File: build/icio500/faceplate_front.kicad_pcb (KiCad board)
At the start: 2 copper layers, 38.1 x 133.3 mm, 3 parts, among them U2 PinHeader_2x07_P2.54mm_Vertic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, U4 TSSOP-24_4.4x7.8mm_P0.65mm

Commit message: faceplate mockupo
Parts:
- removed C3: C_0603_1608Metric, C_0603_1608Metric
- removed U2: PinHeader_2x07_P2.54mm_Vertical, PinHeader_2x07_P2.54mm_Vertical
- removed U4: TSSOP-24_4.4x7.8mm_P0.65mm, TSSOP-24_4.4x7.8mm_P0.65mm
- added ?: , EncoderGraphicGeometric, F.Cu at (19.1, 109.3)
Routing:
- removed copper zone on F.Cu, net (none)
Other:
- copper layers 2 -> 4
- board text removed: "A"
- board text removed: "B"
- board text removed: "G"
- board text removed: "MODE"
- board text removed: "R"
- board text removed: "SEQ"
- board text removed: "SHIFT"
- board text removed: "SYNC"
- board text removed: "TAP / TEMPO"

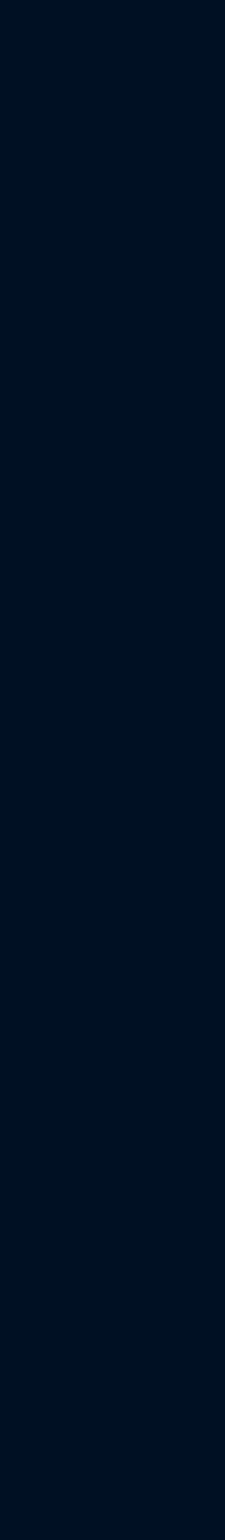
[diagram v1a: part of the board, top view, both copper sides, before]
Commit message: Clean up repo, add mounting holes to faceplate for mating, and assign nets/zones on satellite board via python
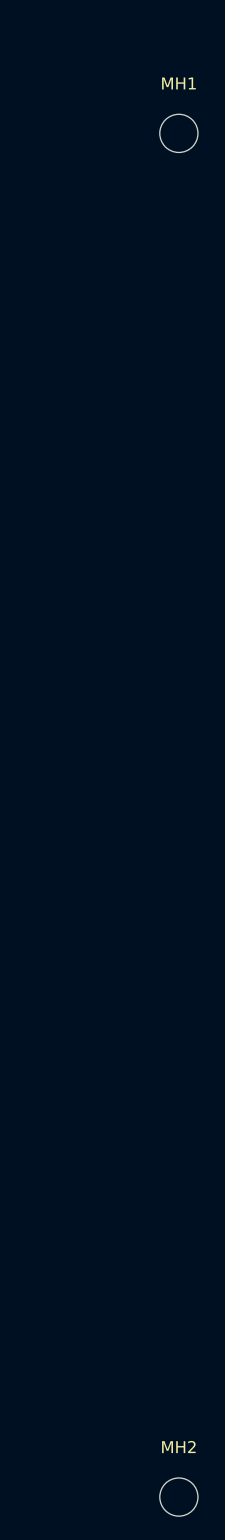
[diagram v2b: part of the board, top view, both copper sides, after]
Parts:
- added MH1: MountingHole_3.2mm_M3, MountingHole_3.2mm_M3, F.Cu at (119.0, 109.5)
- added MH2: MountingHole_3.2mm_M3, MountingHole_3.2mm_M3, F.Cu at (119.0, 223.8)
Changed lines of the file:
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@@
 		)
+	)
+	(footprint "MountingHole_3.2mm_M3"
+		(layer "F.Cu")
+		(at 119.05 109.5)
+		(descr "Mounting Hole 3.2mm, M3, no annular, generated by kicad-footprint-generator mountinghole.py")
+		(tags "mountinghole M3")
+		(property "Reference" "MH1"
+			(at 0 -4.15 0)
+			(layer "F.SilkS")
+			(effects
+				(font
+					(size 1 1)
+					(thickness 0.15)
+				)
+			)
+		)
+		(property "Value" "MountingHole_3.2mm_M3"
+			(at 0 4.15 0)
+			(layer "F.Fab")
+			(effects
+				(font
+					(size 1 1)
+					(thickness 0.15)
+				)
+			)
+		)
+		(property "Datasheet" ""
+			(at 0 0 0)
+			(layer "F.Fab")
+			(hide yes)
+			(effects
+				(font
+					(size 1.27 1.27)
+				)
+			)
+		)
+		(property "Description" ""
+			(at 0 0 0)
+			(layer "F.Fab")
+			(hide yes)
+			(effects
+				(font
+					(size 1.27 1.27)
+				)
+			)
+		)
+		(property "KiLib_Generator" "mounting_hardware/mounting_hole"
+			(at 0 0 0)
+			(layer "F.SilkS")
+			(hide yes)
+			(effects
+				(font
+					(size 1 1)
+					(thickness 0.15)
+				)
+			)
+		)
+		(attr exclude_from_pos_files exclude_from_bom)
+		(duplicate_pad_numbers_are_jumpers no)
+		(fp_circle
+			(center 0 0)
+			(end 3.2 0)
+			(stroke
+				(width 0.15)
+				(type solid)
+			)
+			(fill no)
+			(layer "Cmts.User")
+		)
+		(fp_circle
+			(center 0 0)
+			(end 3.45 0)
+			(stroke
+				(width 0.05)
+				(type solid)
+			)
+			(fill no)
+			(layer "F.CrtYd")
+		)
+		(fp_text user "${REFERENCE}"
+			(at 0 0 0)
+			(layer "F.Fab")
+			(effects
+				(font
+					(size 1 1)
+					(thickness 0.15)
+				)
+			)
+		)
+		(pad "" np_thru_hole circle
+			(at 0 0)
+			(size 3.2 3.2)
+			(drill 3.2)
+			(layers "*.Cu" "*.Mask")
+		)
+		(embedded_fonts no)
 	)
 	(footprint "EncoderGraphicGeometric"
@@
 		)
 		(embedded_fonts no)
+	)
+	(footprint "MountingHole_3.2mm_M3"
+		(layer "F.Cu")
+		(at 119.05 223.85)
+		(descr "Mounting Hole 3.2mm, M3, no annular, generated by kicad-footprint-generator mountinghole.py")
+		(tags "mountinghole M3")
+		(property "Reference" "MH2"
+			(at 0 -4.15 0)
+			(layer "F.SilkS")
+			(effects
+				(font
+					(size 1 1)
+					(thickness 0.15)
+				)
+			)
+		)
+		(property "Value" "MountingHole_3.2mm_M3"
+			(at 0 4.15 0)
+			(layer "F.Fab")
+			(effects
+				(font
+					(size 1 1)
+					(thickness 0.15)
+				)
+			)
+		)
+		(property "Datasheet" ""
+			(at 0 0 0)
+			(layer "F.Fab")
+			(hide yes)
+			(effects
+				(font
+					(size 1.27 1.27)
+				)
+			)
+		)
+		(property "Description" ""
+			(at 0 0 0)
+			(layer "F.Fab")
+			(hide yes)
+			(effects
+				(font
+					(size 1.27 1.27)
+				)
+			)
+		)
+		(property "KiLib_Generator" "mounting_hardware/mounting_hole"
+			(at 0 0 0)
+			(layer "F.SilkS")
+			(hide yes)
+			(effects
+				(font
+					(size 1 1)
+					(thickness 0.15)
+				)
+			)
+		)
+		(attr exclude_from_pos_files exclude_from_bom)
+		(duplicate_pad_numbers_are_jumpers no)
+		(fp_circle
+			(center 0 0)
+			(end 3.2 0)
+			(stroke
+				(width 0.15)
+				(type solid)
+			)
+			(fill no)
+			(layer "Cmts.User")
+		)
+		(fp_circle
+			(center 0 0)
+			(end 3.45 0)
+			(stroke
+				(width 0.05)
+				(type solid)
+			)
+			(fill no)
+			(layer "F.CrtYd")
+		)
+		(fp_text user "${REFERENCE}"
+			(at 0 0 0)
+			(layer "F.Fab")
+			(effects
+				(font
+					(size 1 1)
+					(thickness 0.15)
+				)
+			)
+		)
+		(pad "" np_thru_hole circle
+			(at 0 0)
+			(size 3.2 3.2)
+			(drill 3.2)
+			(layers "*.Cu" "*.Mask")
+		)
+		(embedded_fonts no)

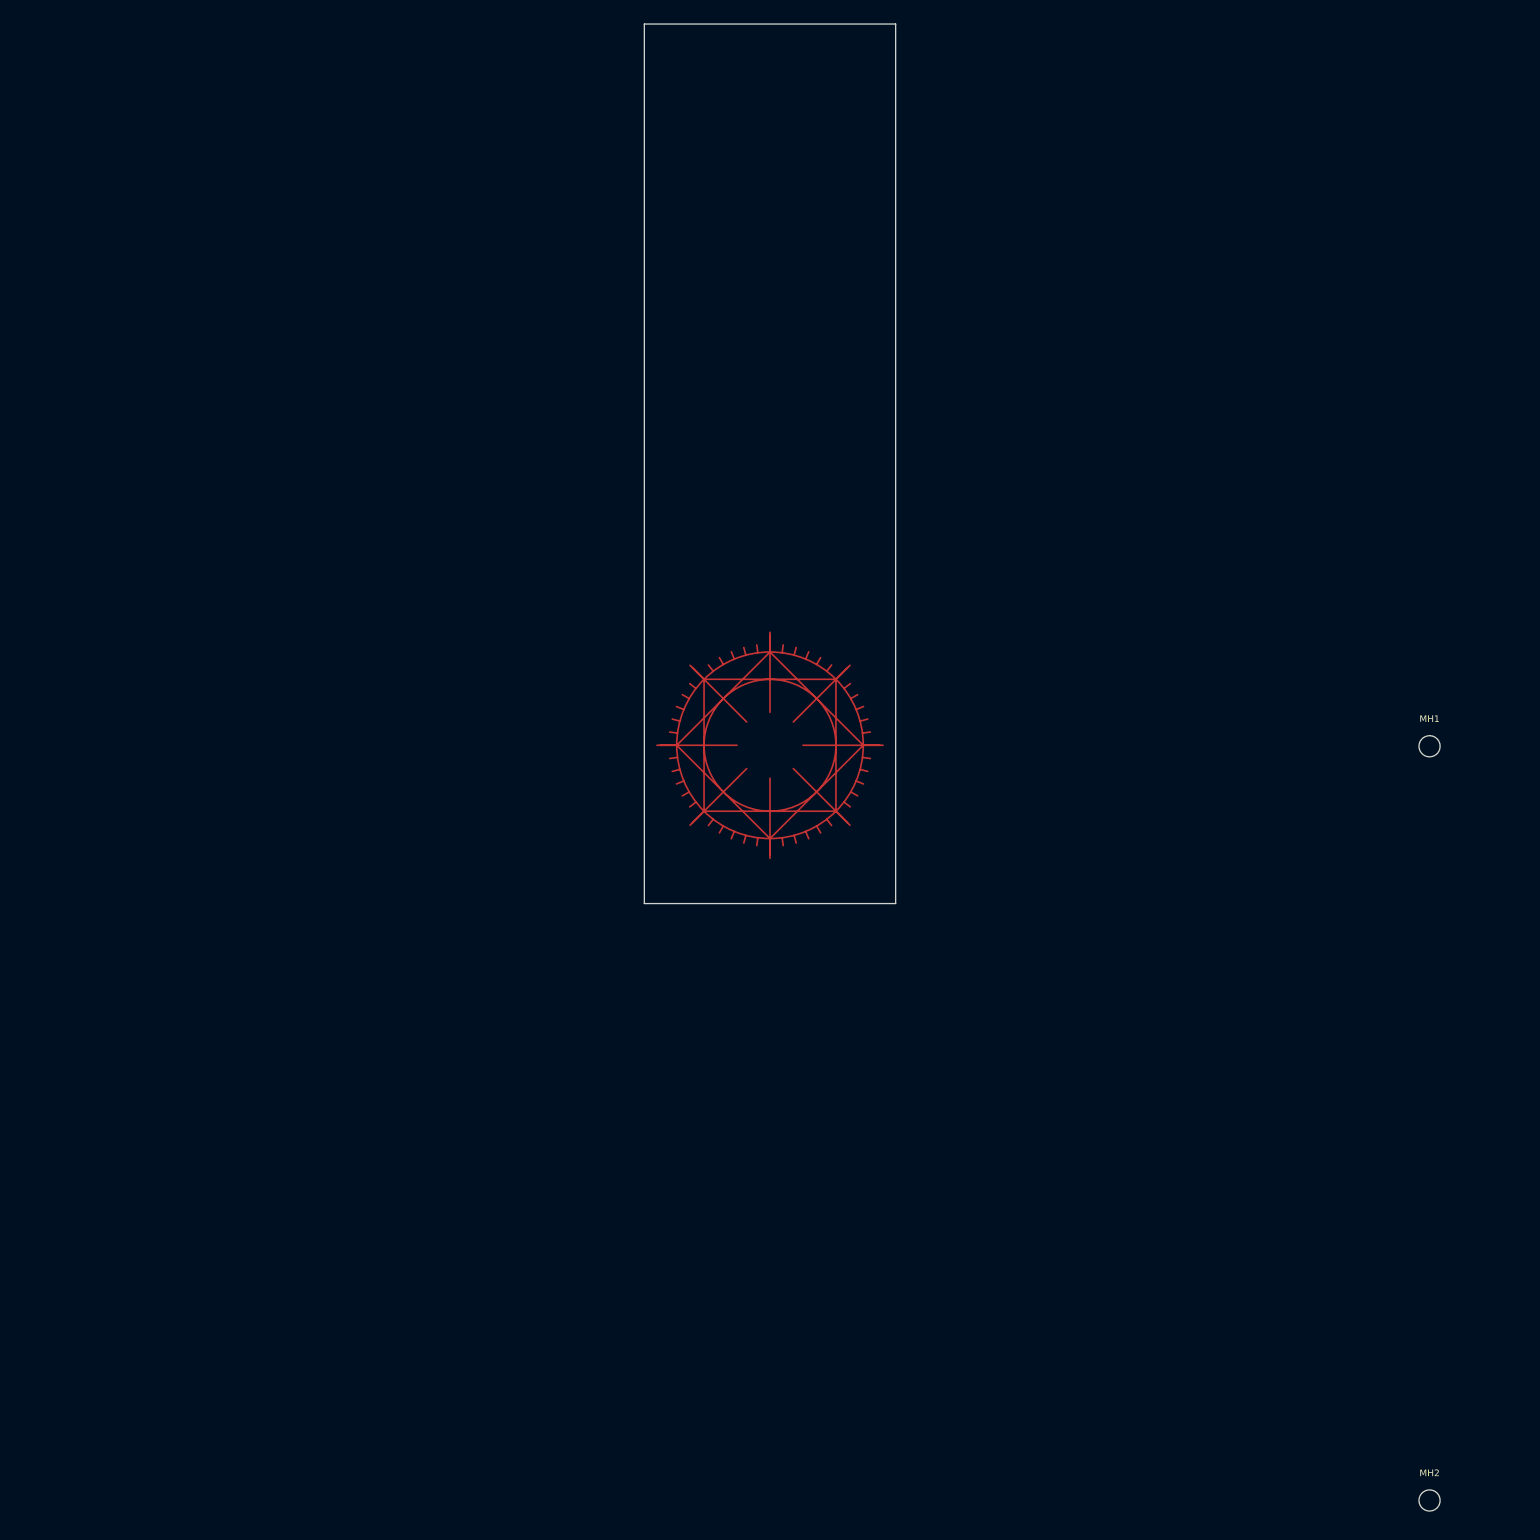
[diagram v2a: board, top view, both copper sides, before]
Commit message: Finalize VPR-500 dimensions and faceplate silkscreen
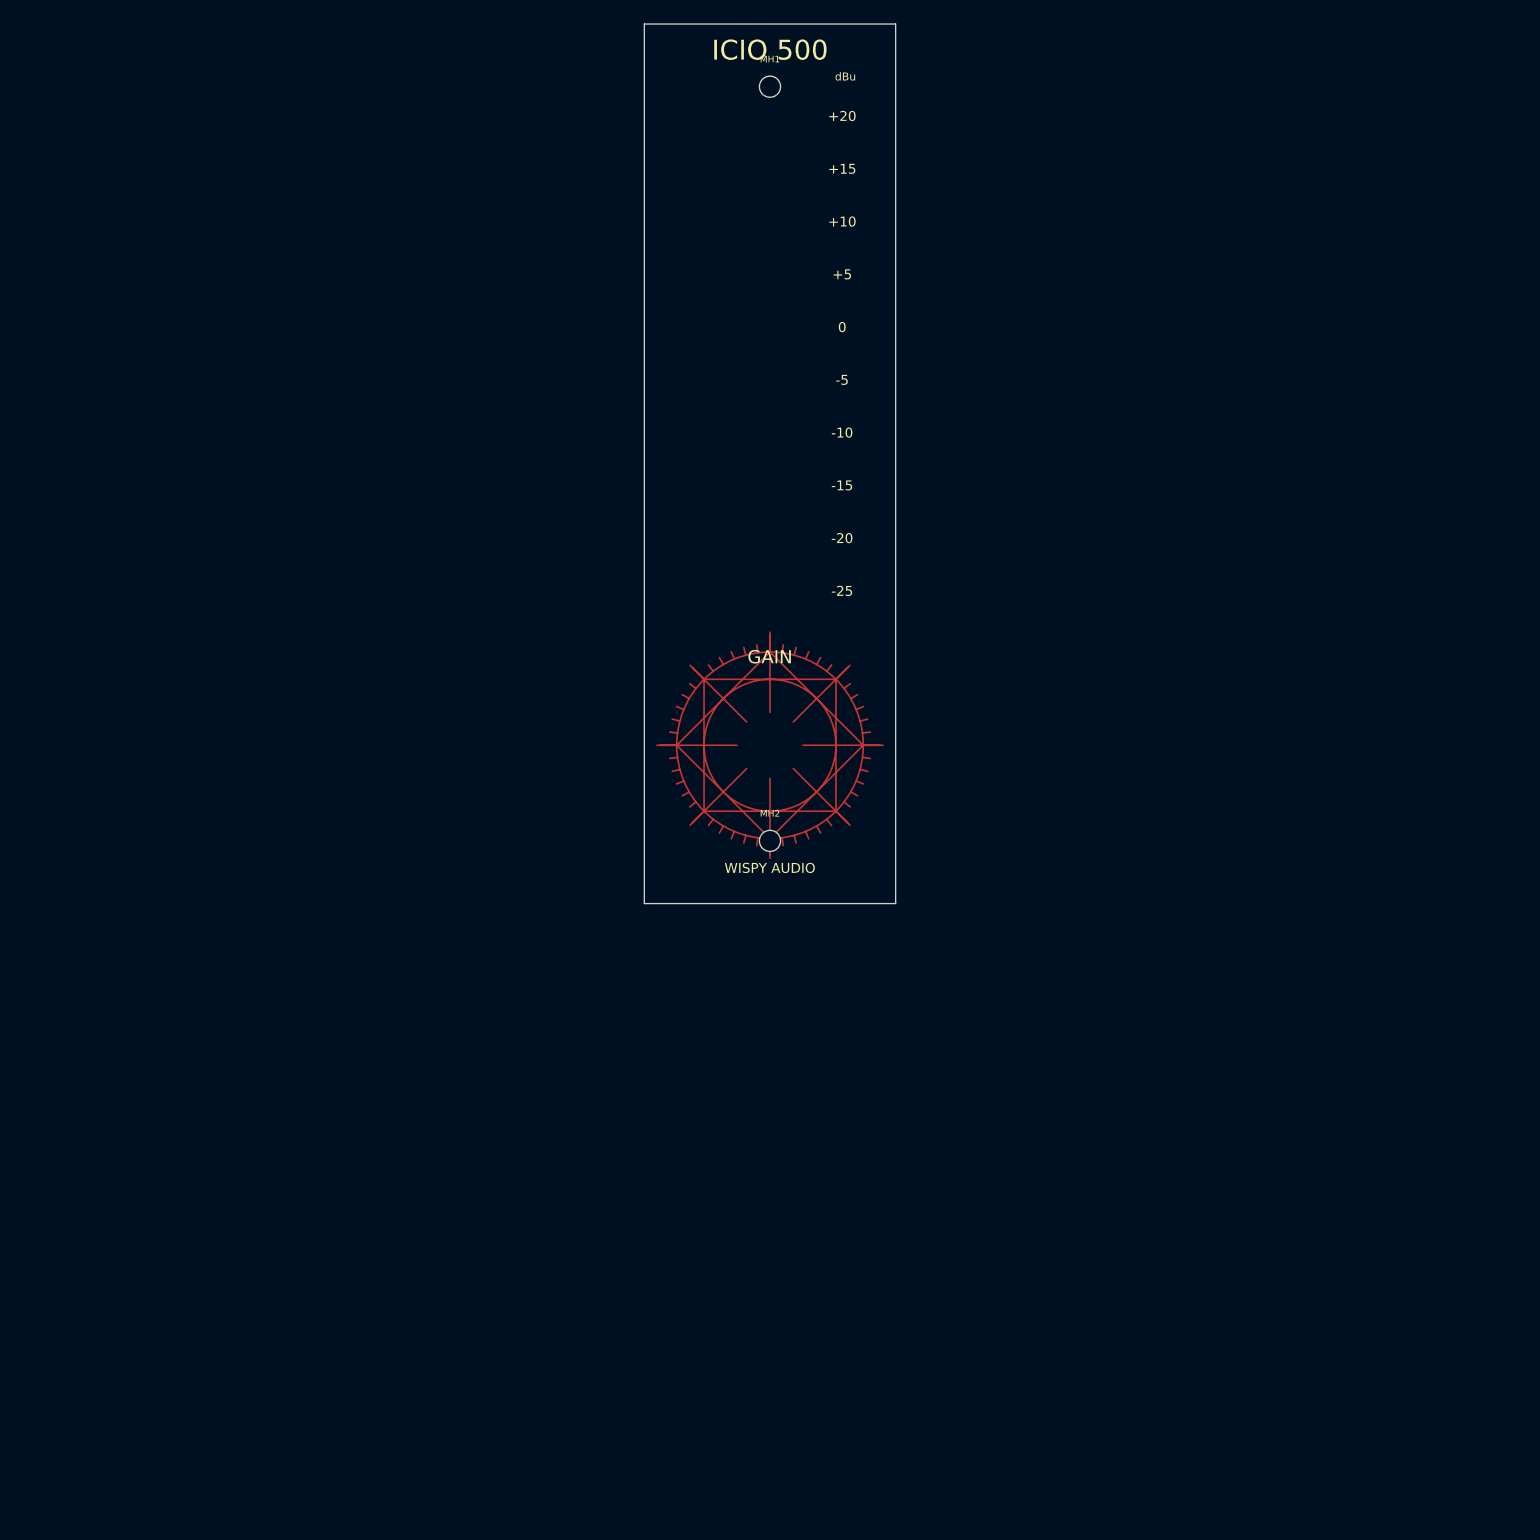
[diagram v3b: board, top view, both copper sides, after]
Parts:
- moved MH1 141.4 mm to (19.1, 9.50)
- moved MH2 141.4 mm to (19.1, 123.8)
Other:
- board text added: "+10"
- board text added: "+15"
- board text added: "+20"
- board text added: "+5"
- board text added: "-10"
- board text added: "-15"
- board text added: "-20"
- board text added: "-25"
- board text added: "-5"
- board text added: "0"
- board text added: "GAIN"
- board text added: "ICIO 500"
- board text added: "WISPY AUDIO"
- board text added: "dBu"
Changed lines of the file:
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@@
 	(footprint "MountingHole_3.2mm_M3"
 		(layer "F.Cu")
-		(at 119.05 109.5)
+		(at 19.05 9.5)
 		(descr "Mounting Hole 3.2mm, M3, no annular, generated by kicad-footprint-generator mountinghole.py")
 		(tags "mountinghole M3")
@@
 	(footprint "MountingHole_3.2mm_M3"
 		(layer "F.Cu")
-		(at 119.05 223.85)
+		(at 19.05 123.85)
 		(descr "Mounting Hole 3.2mm, M3, no annular, generated by kicad-footprint-generator mountinghole.py")
 		(tags "mountinghole M3")
@@
 		(layer "Edge.Cuts")
 	)
+	(gr_text "ICIO 500"
+		(at 19.05 4 0)
+		(layer "F.SilkS")
+		(effects
+			(font
+				(size 3 3)
+				(thickness 0.5)
+			)
+		)
+	)
+	(gr_text "dBu"
+		(at 30.5 8 0)
+		(layer "F.SilkS")
+		(effects
+			(font
+				(size 1.2 1.2)
+				(thickness 0.15)
+			)
+		)
+	)
+	(gr_text "+20"
+		(at 30 14 0)
+		(layer "F.SilkS")
+		(effects
+			(font
+				(size 1.5 1.5)
+				(thickness 0.2)
+			)
+		)
+	)
+	(gr_text "+15"
+		(at 30 22 0)
+		(layer "F.SilkS")
+		(effects
+			(font
+				(size 1.5 1.5)
+				(thickness 0.2)
+			)
+		)
+	)
+	(gr_text "+10"
+		(at 30 30 0)
+		(layer "F.SilkS")
+		(effects
+			(font
+				(size 1.5 1.5)
+				(thickness 0.2)
+			)
+		)
+	)
+	(gr_text "+5"
+		(at 30 38 0)
+		(layer "F.SilkS")
+		(effects
+			(font
+				(size 1.5 1.5)
+				(thickness 0.2)
+			)
+		)
+	)
+	(gr_text "0"
+		(at 30 46 0)
+		(layer "F.SilkS")
+		(effects
+			(font
+				(size 1.5 1.5)
+				(thickness 0.2)
+			)
+		)
+	)
+	(gr_text "-5"
+		(at 30 54 0)
+		(layer "F.SilkS")
+		(effects
+			(font
+				(size 1.5 1.5)
+				(thickness 0.2)
+			)
+		)
+	)
+	(gr_text "-10"
+		(at 30 62 0)
+		(layer "F.SilkS")
+		(effects
+			(font
+				(size 1.5 1.5)
+				(thickness 0.2)
+			)
+		)
+	)
+	(gr_text "-15"
+		(at 30 70 0)
+		(layer "F.SilkS")
+		(effects
+			(font
+				(size 1.5 1.5)
+				(thickness 0.2)
+			)
+		)
+	)
+	(gr_text "-20"
+		(at 30 78 0)
+		(layer "F.SilkS")
+		(effects
+			(font
+				(size 1.5 1.5)
+				(thickness 0.2)
+			)
+		)
+	)
+	(gr_text "-25"
+		(at 30 86 0)
+		(layer "F.SilkS")
+		(effects
+			(font
+				(size 1.5 1.5)
+				(thickness 0.2)
+			)
+		)
+	)
+	(gr_text "GAIN"
+		(at 19.05 96 0)
+		(layer "F.SilkS")
+		(effects
+			(font
+				(size 2 2)
+				(thickness 0.3)
+			)
+		)
+	)
+	(gr_text "WISPY AUDIO"
+		(at 19.05 128 0)
+		(layer "F.SilkS")
+		(effects
+			(font
+				(size 1.5 1.5)
+				(thickness 0.2)
+			)
+		)
+	)
 	(embedded_fonts no)
